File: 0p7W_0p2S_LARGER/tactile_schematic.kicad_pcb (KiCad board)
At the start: 2 copper layers, 145.2 x 85.6 mm, 55 parts, among them IC1 CY8C4145PVI-PS431, J1 Conn_01x03, J2 Conn_01x04, J3 Conn_01x04, J4 Conn_01x03, J5 Conn_ARM_SWD_TagConnect_TC203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

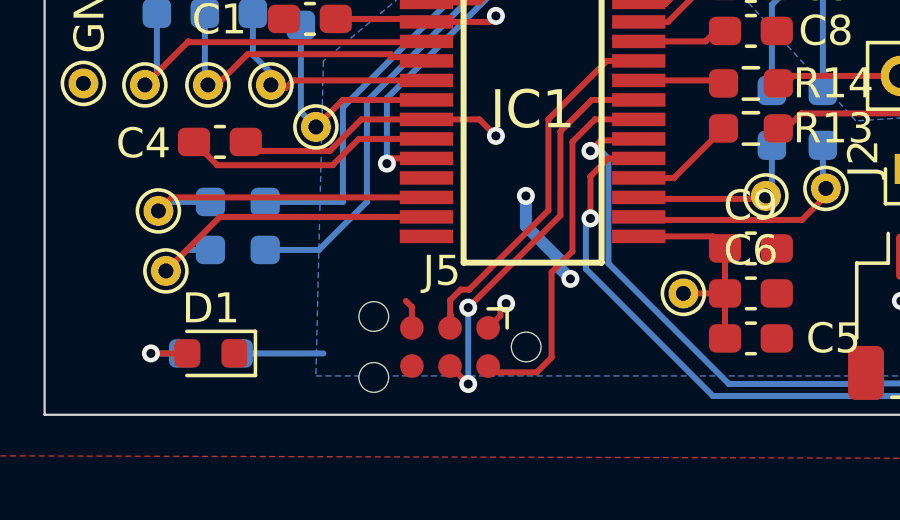
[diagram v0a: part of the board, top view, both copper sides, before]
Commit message: move prog connector up, make bottom of gnd plane connected propelrly
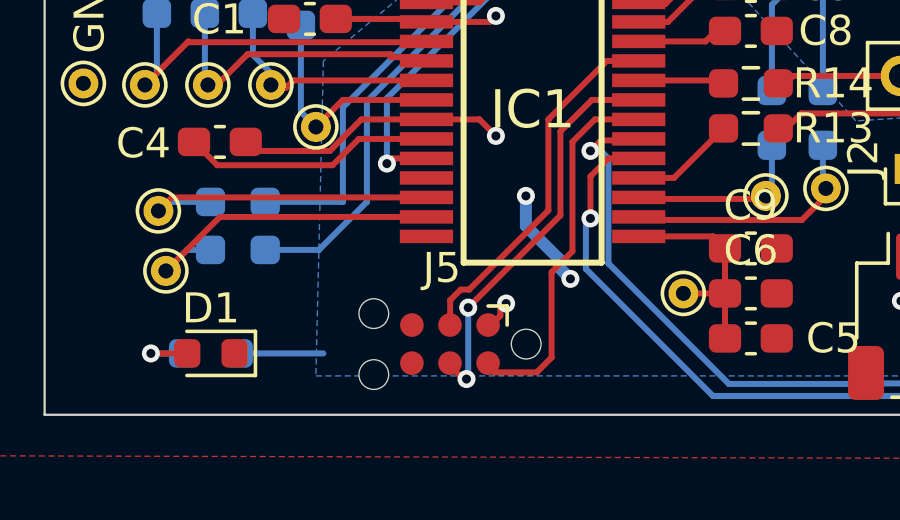
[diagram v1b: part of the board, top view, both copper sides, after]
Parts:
- moved J5 0.10 mm to (111.5, 126.9)
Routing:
- net GND: track 25.4 -> 24.4 mm
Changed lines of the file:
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@@
 	(footprint "Connector:Tag-Connect_TC2030-IDC-NL_2x03_P1.27mm_Vertical"
 		(layer "F.Cu")
-		(at 111.545603 127.031125 180)
+		(at 111.545603 126.935 180)
 		(descr "Tag-Connect programming header; http://www.tag-connect.com/Materials/TC2030-IDC-NL.pdf")
 		(tags "tag connect programming header pogo pins")
@@
 			(polygon
 				(pts
-					(xy 110.275603 127.666125) (xy 112.815603 127.666125) (xy 112.815603 126.396125) (xy 110.275603 126.396125)
+					(xy 110.275603 127.57) (xy 112.815603 127.57) (xy 112.815603 126.3) (xy 110.275603 126.3)
 				)
 			)
@@
 	)
 	(segment
-		(start 110.275603 125.696125)
-		(end 110.075603 125.496125)
-		(width 0.2)
-		(layer "F.Cu")
-		(net 2)
-	)
-	(segment
 		(start 108.508389 120.096125)
 		(end 107.632389 120.972125)
@@
 		(net 2)
 	)
-	(segment
-		(start 110.275603 126.396125)
-		(end 110.275603 125.696125)
-		(width 0.2)
-		(layer "F.Cu")
-		(net 2)
-	)
 	(via
 		(at 114.075603 121.996125)
@@
 	)
 	(segment
-		(start 111.55329 127.666125)
-		(end 112.152973 128.265808)
+		(start 116.275603 118.796125)
+		(end 117.837108 118.796125)
 		(width 0.2)
 		(layer "F.Cu")
@@
 	)
 	(segment
-		(start 116.275603 118.796125)
-		(end 117.837108 118.796125)
+		(start 112.082951 128.113396)
+		(end 112.000561 128.113396)
 		(width 0.2)
 		(layer "F.Cu")
@@
 	)
 	(segment
+		(start 112.096157 128.10019)
+		(end 112.082951 128.113396)
+		(width 0.2)
+		(layer "F.Cu")
+		(net 22)
+	)
+	(segment
 		(start 115.226603 122.645125)
 		(end 115.226603 119.845125)
@@
 	)
 	(segment
+		(start 111.55329 127.666125)
+		(end 111.545603 127.666125)
+		(width 0.2)
+		(layer "F.Cu")
+		(net 22)
+	)
+	(segment
 		(start 112.152973 125.718755)
 		(end 115.226603 122.645125)
@@
 	)
 	(segment
-		(start 111.545603 127.666125)
+		(start 112.000561 128.113396)
 		(end 111.55329 127.666125)
 		(width 0.2)
@@
 	)
 	(via
-		(at 112.152973 128.265808)
+		(at 112.096157 128.10019)
 		(size 0.6)
 		(drill 0.3)
@@
 	)
 	(segment
-		(start 112.152973 125.718755)
-		(end 112.152973 128.265808)
+		(start 112.096157 128.10019)
+		(end 112.119284 128.10019)
+		(width 0.2)
+		(layer "B.Cu")
+		(net 22)
+	)
+	(segment
+		(start 112.152973 128.066501)
+		(end 112.152973 125.718755)
+		(width 0.2)
+		(layer "B.Cu")
+		(net 22)
+	)
+	(segment
+		(start 112.119284 128.10019)
+		(end 112.152973 128.066501)
 		(width 0.2)
 		(layer "B.Cu")
